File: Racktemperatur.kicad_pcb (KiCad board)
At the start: 2 copper layers, 67.6 x 57.5 mm, 20 parts, among them J1 Conn_01x03, J2 Conn_01x03, J3 Barrel_Jack_MountingPin, Q1 IRLZ44N, U1 74HC595, U2 74HC595, U3 DS18B20

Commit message: Version 1.3 as rack mount
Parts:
- removed the REF** at (145.7, 125.5)
- removed the REF** at (84.4, 125.5)
- added G***: LOGO, libs:Logo, F.Cu at (111.7, 101.7)
- added J4: Screw_Terminal_01x02, TerminalBlock:TerminalBlock_bornier-2_P5.08mm, F.Cu at (187.8, 91.1)
- R1, R2, R3, R4, R5: moved to B.Cu
- moved J3 83.1 mm to (177.9, 98.9), turned to 90 degrees
- moved R4 78.7 mm to (180.1, 117.3)
- moved REF** 65.0 mm to (190.0, 115.4)
- moved R5 61.7 mm to (175.0, 117.3), turned to 90 degrees
- moved R3 58.1 mm to (180.3, 90.8), turned to 180 degrees
- moved U3 56.7 mm to (178.9, 87.5), turned to 0 degrees
- moved U1 56.6 mm to (137.0, 82.8), turned to 0 degrees
- moved J2 52.8 mm to (163.8, 91.8), turned to 270 degrees
- moved J1 52.6 mm to (163.8, 82.9), turned to 270 degrees
- moved U2 52.0 mm to (123.3, 82.8), turned to 0 degrees
- moved Q1 48.8 mm to (151.1, 101.0), turned to 0 degrees
- moved A1 47.6 mm to (152.1, 120.9), turned to 90 degrees
- moved D1 43.8 mm to (164.7, 101.3), turned to 180 degrees
- moved R1 21.2 mm to (140.8, 116.6)
- moved G*** 20.7 mm to (111.7, 101.7), turned to 180 degrees
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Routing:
- net GND: track 66.4 -> 27.7 mm, vias 0 -> 5
- net Net-(A1-Pad27): track 38.8 -> 3.35 mm, vias 1 -> 0
- net Net-(A1-Pad15): track 95.2 -> 60.7 mm, vias 2 -> 1
- net Net-(A1-Pad16): track 0.00 -> 21.1 mm
- net Net-(A1-Pad5): track 24.7 -> 3.67 mm
- net +12V: track 67.6 -> 49.0 mm
- net Net-(A1-Pad10): track 19.7 -> 2.53 mm
- net Net-(D1-Pad2): track 3.26 -> 20.3 mm
- net Net-(A1-Pad13): track 82.3 -> 68.1 mm, vias 0 -> 1
- net Net-(A1-Pad14): track 83.9 -> 70.0 mm, vias 2 -> 0
- net Net-(U1-Pad9): track 19.9 -> 29.6 mm, vias 0 -> 2
- net Net-(A1-Pad17): track 111.4 -> 102.6 mm, vias 0 -> 2
- net Net-(J1-Pad1): track 17.4 -> 24.4 mm
- net Net-(A1-Pad12): track 38.7 -> 45.0 mm, vias 1 -> 3
- net Net-(AFF2-Pad2): track 31.1 -> 34.3 mm
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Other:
- board size 67.6 x 57.5 mm -> 91.8 x 42.7 mm
- board text added: "D2 = DS18B20 1Wire Sensor D7 = LED D9 = Fan PWM (MOSFET) D10 = 7 Seg RCLK D11 = 7 Seg SRCLK D12 = 7 Seg SER D13 = Terminal"
- board text added: "IRLZ44N"
- board text added: "v1.3"
- board text removed: "D2 = DS18B20 1Wire Sensor D7 = LED D9 = Fan PWM (MOSFET) D10 = 7 Seg RCLK D11 = 7 Seg SRCLK D12 = 7 Seg SER"
- board text removed: "v1.2"

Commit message: unconnected item
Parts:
- added REF**: WEEE-Logo_4.2x6mm_SilkScreen, Symbol:WEEE-Logo_4.2x6mm_SilkScreen, F.Cu at (172.0, 88.4)
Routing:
- net Net-(A1-Pad5): track 3.67 -> 48.7 mm, vias 0 -> 2
- net Net-(A1-Pad27): track 3.35 -> 31.8 mm, vias 0 -> 1
- net GND: vias 5 -> 6
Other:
- board text added: "v1.4"
- board text removed: "v1.3"

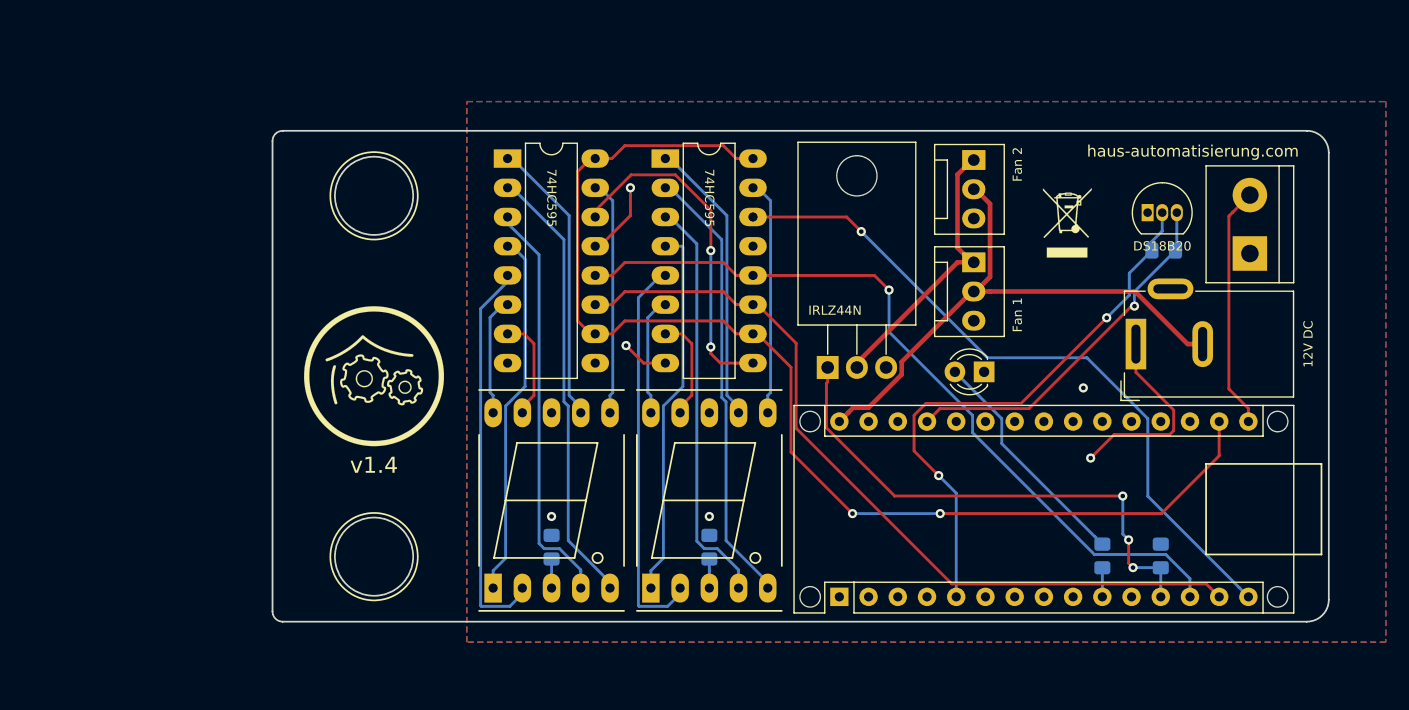
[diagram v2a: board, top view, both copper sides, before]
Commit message: Added LM7805
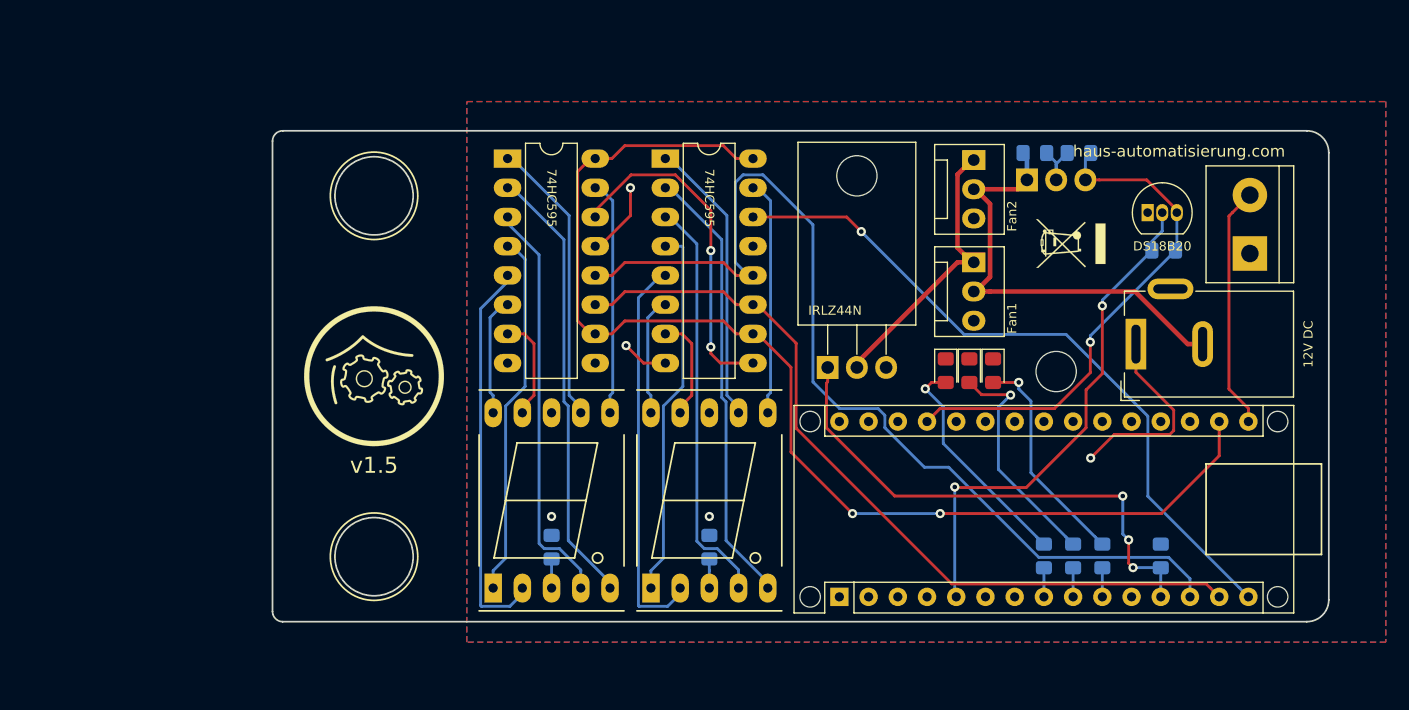
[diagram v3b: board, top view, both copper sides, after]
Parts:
- added C1: C, Capacitor_SMD:C_0805_2012Metric_Pad1.15x1.40mm_HandSolder, B.Cu at (169.1, 82.3)
- added C2: C, Capacitor_SMD:C_0805_2012Metric_Pad1.15x1.40mm_HandSolder, B.Cu at (173.0, 82.3)
- added D2: LED, LED_SMD:LED_0805_2012Metric_Pad1.15x1.40mm_HandSolder, F.Cu at (161.4, 101.2)
- added D3: LED, LED_SMD:LED_0805_2012Metric_Pad1.15x1.40mm_HandSolder, F.Cu at (163.4, 101.2)
- added R6: 330Ω, Resistor_SMD:R_0805_2012Metric_Pad1.15x1.40mm_HandSolder, B.Cu at (169.9, 117.3)
- added R7: 330Ω, Resistor_SMD:R_0805_2012Metric_Pad1.15x1.40mm_HandSolder, B.Cu at (172.5, 117.3)
- added U4: L7805, Package_TO_SOT_THT:TO-220-3_Horizontal_TabDown, B.Cu at (168.5, 84.7)
- D1: footprint LED_THT:LED_D3.0mm -> LED_SMD:LED_0805_2012Metric_Pad1.15x1.40mm_HandSolder
- moved REF** 2.31 mm to (190.3, 113.2)
- moved REF** 1.83 mm to (172.3, 90.2), turned to 90 degrees
- moved D1 0.78 mm to (165.5, 101.2), turned to 270 degrees
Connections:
- net Net-(A1-Pad17) renamed /3V3
- net Net-(A1-Pad27) renamed /5V
- A1 pad 30: +12V -> Net-(A1-Pad30)
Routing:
- net Net-(D3-Pad2): track 0.00 -> 20.1 mm, vias 0 -> 1
- net Net-(A1-Pad13): track 68.1 -> 88.1 mm, vias 1 -> 0
- net Net-(D2-Pad2): track 0.00 -> 19.8 mm, vias 0 -> 1
- net /5V: track 31.8 -> 44.8 mm
- net +12V: track 49.0 -> 39.5 mm
- net GND: track 27.7 -> 33.1 mm, vias 6 -> 5
- net Net-(A1-Pad5): track 48.7 -> 44.6 mm
- net Net-(A1-Pad9): track 0.00 -> 2.53 mm
- net Net-(A1-Pad8): track 0.00 -> 2.53 mm
- net Net-(D1-Pad2): track 20.3 -> 19.3 mm, vias 0 -> 1
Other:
- board text added: "100nF"
- board text added: "D2 = DS18B20 1Wire Sensor D5, D7, D7 = LED D9 = Fan PWM (MOSFET) D10 = 7 Seg RCLK D11 = 7 Seg SRCLK D12 = 7 Seg SER D13 = Terminal"
- board text added: "Fan1"
- board text added: "Fan2"
- board text added: "LM7805"
- board text added: "v1.5"
- board text removed: "D2 = DS18B20 1Wire Sensor D7 = LED D9 = Fan PWM (MOSFET) D10 = 7 Seg RCLK D11 = 7 Seg SRCLK D12 = 7 Seg SER D13 = Terminal"
- board text removed: "Fan 1"
- board text removed: "Fan 2"
- board text removed: "v1.4"

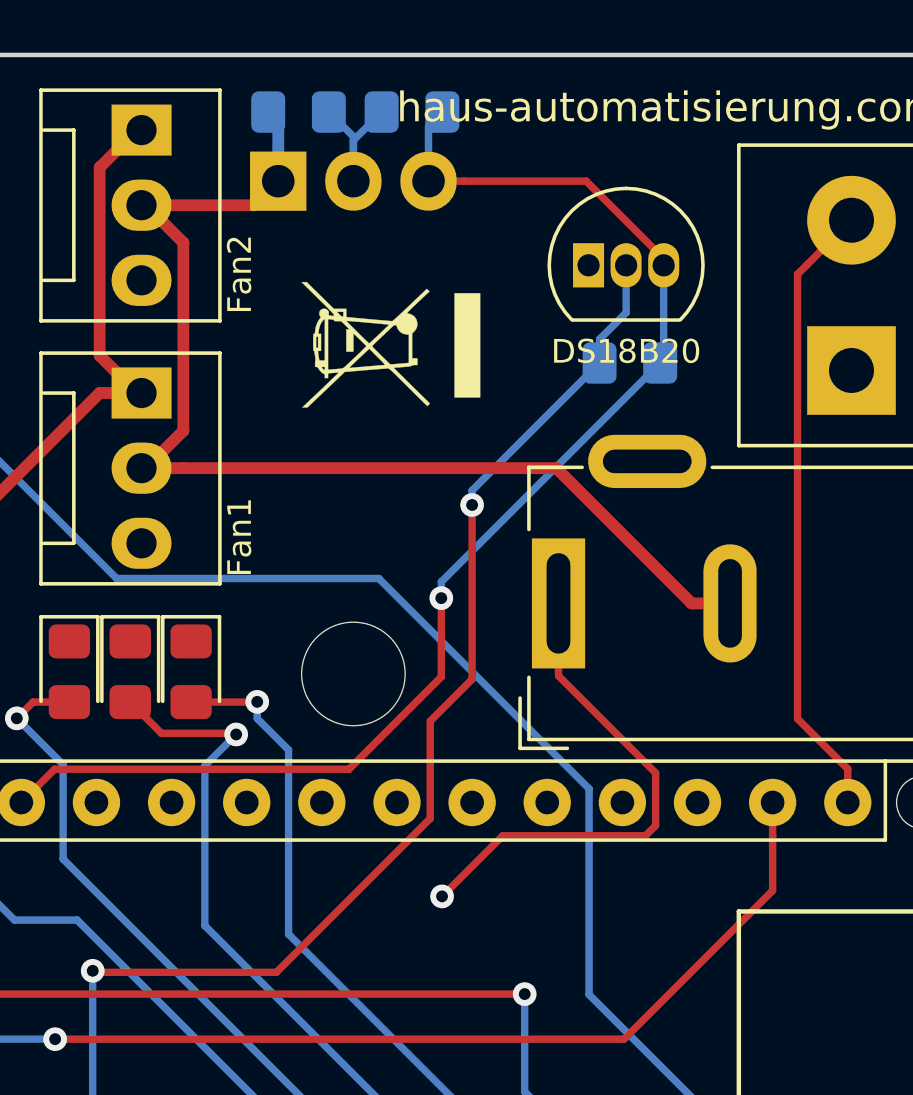
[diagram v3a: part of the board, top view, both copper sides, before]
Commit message: Changed polarity of barrel jack
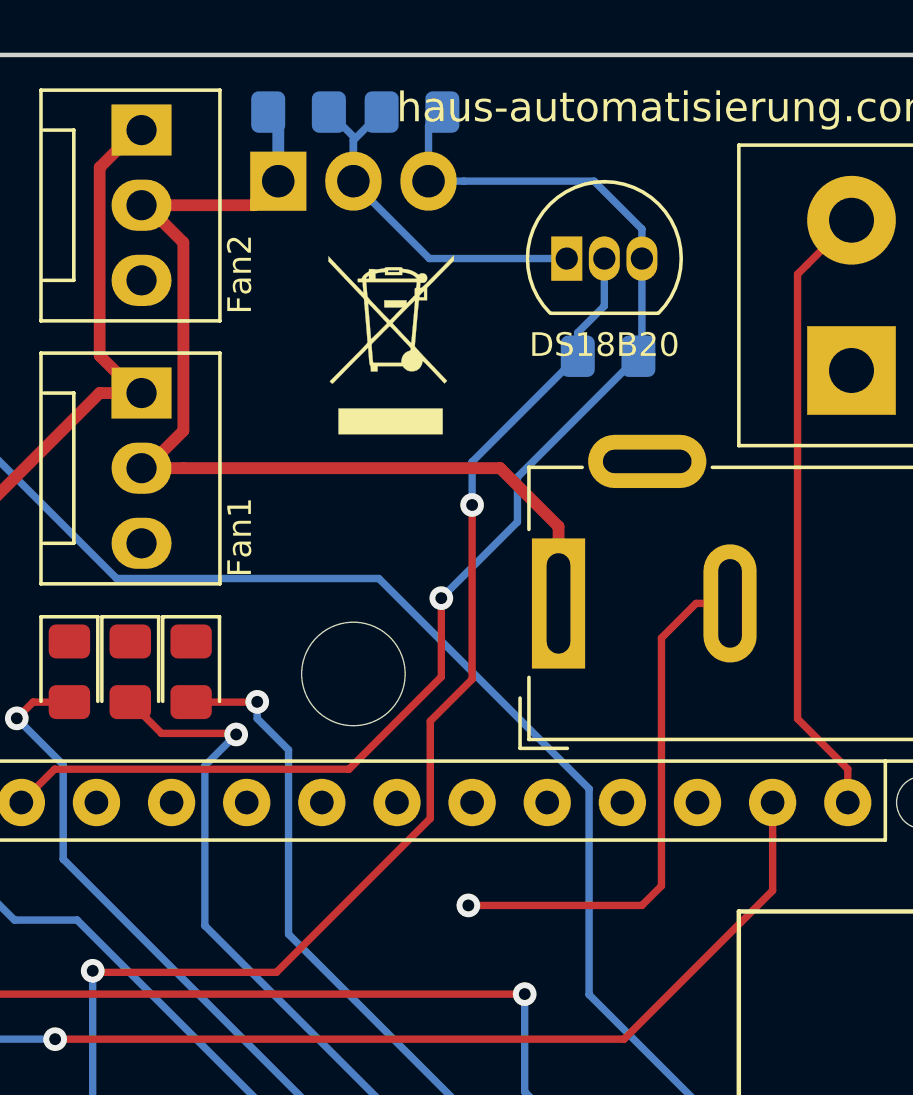
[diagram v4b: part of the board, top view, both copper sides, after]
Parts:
- moved R3 0.77 mm to (179.6, 90.6)
- moved U3 0.77 mm to (178.2, 87.3)
- turned REF** to 0 degrees
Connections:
- J3 pad 1: GND -> +12V
- J3 pad 2: +12V -> GND
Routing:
- net GND: track 33.1 -> 42.4 mm
- net +12V: track 39.5 -> 35.2 mm
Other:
- board text added: "D2 = DS18B20 1Wire Sensor D5, D7, D7 = LED D9 = Fan PWM D10 = 7 Seg RCLK D11 = 7 Seg SRCLK D12 = 7 Seg SER D13 = Terminal"
- board text removed: "D2 = DS18B20 1Wire Sensor D5, D7, D7 = LED D9 = Fan PWM (MOSFET) D10 = 7 Seg RCLK D11 = 7 Seg SRCLK D12 = 7 Seg SER D13 = Terminal"

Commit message: Minor changes
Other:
- board text added: "R Y G"
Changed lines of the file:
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@@
   (general
     (thickness 1.6)
-    (drawings 46)
+    (drawings 47)
     (tracks 304)
     (zones 0)
@@
   (title_block
     (title "Rack Temperature Control")
-    (date 2019-10-26)
+    (date 2019-11-12)
     (rev 1.5)
     (company haus-automatisierung.com)
@@
     )
   )
+  (gr_text "R    Y    G" (at 163.449 103.6828) (layer F.SilkS)
+    (effects (font (size 0.5 0.5) (thickness 0.125)))
+  )
   (gr_text 100nF (at 166.5732 83.185 90) (layer B.SilkS)

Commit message: Added Source Code
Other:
- board text added: "D2 = DS18B20 1Wire Sensor D5, D6, D7 = LED D9 = Fan PWM D10 = 7 Seg RCLK D11 = 7 Seg SRCLK D12 = 7 Seg SER D13 = Terminal"
- board text removed: "D2 = DS18B20 1Wire Sensor D5, D7, D7 = LED D9 = Fan PWM D10 = 7 Seg RCLK D11 = 7 Seg SRCLK D12 = 7 Seg SER D13 = Terminal"
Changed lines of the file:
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@@
     (effects (font (size 0.8 0.8) (thickness 0.15)) (justify mirror))
   )
-  (gr_text "D2 = DS18B20 1Wire Sensor\nD5, D7, D7 = LED\nD9 = Fan PWM\nD10 = 7 Seg RCLK\nD11 = 7 Seg SRCLK\nD12 = 7 Seg SER\nD13 = Terminal" (at 151.6634 88.0364 90) (layer B.SilkS)
+  (gr_text "D2 = DS18B20 1Wire Sensor\nD5, D6, D7 = LED\nD9 = Fan PWM\nD10 = 7 Seg RCLK\nD11 = 7 Seg SRCLK\nD12 = 7 Seg SER\nD13 = Terminal" (at 151.6634 88.0364 90) (layer B.SilkS)
     (effects (font (size 0.7 0.7) (thickness 0.15)) (justify left mirror))
   )

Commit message: Updated to KiCad 6
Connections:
- A1 pad 1: Net-(A1-Pad1) -> unconnected-(A1-Pad1)
- A1 pad 11: Net-(A1-Pad11) -> unconnected-(A1-Pad11)
- A1 pad 18: Net-(A1-Pad18) -> unconnected-(A1-Pad18)
- A1 pad 19: Net-(A1-Pad19) -> unconnected-(A1-Pad19)
- A1 pad 2: Net-(A1-Pad2) -> unconnected-(A1-Pad2)
- A1 pad 20: Net-(A1-Pad20) -> unconnected-(A1-Pad20)
- A1 pad 21: Net-(A1-Pad21) -> unconnected-(A1-Pad21)
- A1 pad 22: Net-(A1-Pad22) -> unconnected-(A1-Pad22)
- A1 pad 23: Net-(A1-Pad23) -> unconnected-(A1-Pad23)
- A1 pad 24: Net-(A1-Pad24) -> unconnected-(A1-Pad24)
- A1 pad 25: Net-(A1-Pad25) -> unconnected-(A1-Pad25)
- A1 pad 26: Net-(A1-Pad26) -> unconnected-(A1-Pad26)
- A1 pad 28: Net-(A1-Pad28) -> unconnected-(A1-Pad28)
- A1 pad 29: Net-(A1-Pad29) -> unconnected-(A1-Pad29)
- A1 pad 3: Net-(A1-Pad3) -> unconnected-(A1-Pad3)
- A1 pad 30: Net-(A1-Pad30) -> unconnected-(A1-Pad30)
- A1 pad 6: Net-(A1-Pad6) -> unconnected-(A1-Pad6)
- A1 pad 7: Net-(A1-Pad7) -> unconnected-(A1-Pad7)
- AFF1 pad 8: Net-(AFF1-Pad8) -> unconnected-(AFF1-Pad8)
- AFF2 pad 8: Net-(AFF2-Pad8) -> unconnected-(AFF2-Pad8)
- J1 pad 3: Net-(J1-Pad3) -> unconnected-(J1-Pad3)
- J2 pad 3: Net-(J2-Pad3) -> unconnected-(J2-Pad3)
- U2 pad 9: Net-(U2-Pad9) -> unconnected-(U2-Pad9)
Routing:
- net Net-(A1-Pad14): track 70.0 -> 70.8 mm
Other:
- net class 12V removed
- net class Default removed

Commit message: v1.6
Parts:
- C1, C2: footprint Capacitor_SMD:C_0805_2012Metric_Pad1.15x1.40mm_HandSolder -> Capacitor_SMD:C_0805_2012Metric_Pad1.18x1.45mm_HandSolder
- R1, R2, R3, R4, R5, R6, R7: footprint Resistor_SMD:R_0805_2012Metric_Pad1.15x1.40mm_HandSolder -> Resistor_SMD:R_0805_2012Metric_Pad1.20x1.40mm_HandSolder
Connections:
- A1 pad 1: unconnected-(A1-Pad1) -> (no net)
- A1 pad 10: Net-(A1-Pad10) -> (no net)
- A1 pad 11: unconnected-(A1-Pad11) -> (no net)
- A1 pad 12: Net-(A1-Pad12) -> (no net)
- A1 pad 13: Net-(A1-Pad13) -> (no net)
- A1 pad 14: Net-(A1-Pad14) -> (no net)
- A1 pad 15: Net-(A1-Pad15) -> (no net)
- A1 pad 16: Net-(A1-Pad16) -> (no net)
- A1 pad 18: unconnected-(A1-Pad18) -> (no net)
- A1 pad 19: unconnected-(A1-Pad19) -> (no net)
- A1 pad 2: unconnected-(A1-Pad2) -> (no net)
- A1 pad 20: unconnected-(A1-Pad20) -> (no net)
- A1 pad 21: unconnected-(A1-Pad21) -> (no net)
- A1 pad 22: unconnected-(A1-Pad22) -> (no net)
- A1 pad 23: unconnected-(A1-Pad23) -> (no net)
- A1 pad 24: unconnected-(A1-Pad24) -> (no net)
- A1 pad 25: unconnected-(A1-Pad25) -> (no net)
- A1 pad 26: unconnected-(A1-Pad26) -> (no net)
- A1 pad 28: unconnected-(A1-Pad28) -> (no net)
- A1 pad 29: unconnected-(A1-Pad29) -> (no net)
- A1 pad 3: unconnected-(A1-Pad3) -> (no net)
- A1 pad 30: unconnected-(A1-Pad30) -> (no net)
- A1 pad 5: Net-(A1-Pad5) -> (no net)
- A1 pad 6: unconnected-(A1-Pad6) -> (no net)
- A1 pad 7: unconnected-(A1-Pad7) -> (no net)
- A1 pad 8: Net-(A1-Pad8) -> (no net)
- A1 pad 9: Net-(A1-Pad9) -> (no net)
- AFF1 pad 1: Net-(AFF1-Pad1) -> (no net)
- AFF1 pad 10: Net-(AFF1-Pad10) -> (no net)
- AFF1 pad 2: Net-(AFF1-Pad2) -> (no net)
- AFF1 pad 3: Net-(AFF1-Pad3) -> (no net)
- AFF1 pad 4: Net-(AFF1-Pad4) -> (no net)
- AFF1 pad 5: Net-(AFF1-Pad5) -> (no net)
- AFF1 pad 6: Net-(AFF1-Pad6) -> (no net)
- AFF1 pad 7: Net-(AFF1-Pad7) -> (no net)
- AFF1 pad 8: unconnected-(AFF1-Pad8) -> (no net)
- AFF1 pad 9: Net-(AFF1-Pad9) -> (no net)
- AFF2 pad 1: Net-(AFF2-Pad1) -> (no net)
- AFF2 pad 10: Net-(AFF2-Pad10) -> (no net)
- AFF2 pad 2: Net-(AFF2-Pad2) -> (no net)
- AFF2 pad 3: Net-(AFF2-Pad3) -> (no net)
- AFF2 pad 4: Net-(AFF2-Pad4) -> (no net)
- AFF2 pad 5: Net-(AFF2-Pad5) -> (no net)
- AFF2 pad 6: Net-(AFF2-Pad6) -> (no net)
- AFF2 pad 7: Net-(AFF2-Pad7) -> (no net)
- AFF2 pad 8: unconnected-(AFF2-Pad8) -> (no net)
- AFF2 pad 9: Net-(AFF2-Pad9) -> (no net)
- D1 pad 2: Net-(D1-Pad2) -> (no net)
- D2 pad 2: Net-(D2-Pad2) -> (no net)
- D3 pad 2: Net-(D3-Pad2) -> (no net)
- J1 pad 1: Net-(J1-Pad1) -> (no net)
- J1 pad 3: unconnected-(J1-Pad3) -> (no net)
- J2 pad 1: Net-(J1-Pad1) -> Net-(J1-Pin_1)
- J2 pad 3: unconnected-(J2-Pad3) -> (no net)
- J4 pad 2: Net-(A1-Pad16) -> Net-(A1-D13)
- Q1 pad 1: Net-(A1-Pad12) -> Net-(A1-D9)
- Q1 pad 2: Net-(J1-Pad1) -> Net-(J1-Pin_1)
- R1 pad 1: Net-(AFF1-Pad3) -> Net-(AFF1-C.K.-Pad3)
- R2 pad 1: Net-(AFF2-Pad3) -> Net-(AFF2-C.K.-Pad3)
- R3 pad 2: Net-(A1-Pad5) -> Net-(A1-D2)
- R4 pad 1: Net-(A1-Pad12) -> Net-(A1-D9)
- R5 pad 1: Net-(A1-Pad10) -> Net-(A1-D7)
- R5 pad 2: Net-(D1-Pad2) -> Net-(D1-A)
- R6 pad 1: Net-(A1-Pad8) -> Net-(A1-D5)
- R6 pad 2: Net-(D2-Pad2) -> Net-(D2-A)
- R7 pad 1: Net-(A1-Pad9) -> Net-(A1-D6)
- R7 pad 2: Net-(D3-Pad2) -> Net-(D3-A)
- U1 pad 1: Net-(AFF1-Pad7) -> Net-(AFF1-a)
- U1 pad 11: Net-(A1-Pad14) -> Net-(A1-D11)
- U1 pad 12: Net-(A1-Pad13) -> Net-(A1-D10)
- U1 pad 14: Net-(A1-Pad15) -> Net-(A1-D12)
- U1 pad 15: Net-(AFF1-Pad6) -> Net-(AFF1-b)
- U1 pad 2: Net-(AFF1-Pad5) -> Net-(AFF1-DP)
- U1 pad 3: Net-(AFF1-Pad4) -> Net-(AFF1-c)
- U1 pad 4: Net-(AFF1-Pad1) -> Net-(AFF1-e)
- U1 pad 5: Net-(AFF1-Pad2) -> Net-(AFF1-d)
- U1 pad 6: Net-(AFF1-Pad10) -> Net-(AFF1-g)
- U1 pad 7: Net-(AFF1-Pad9) -> Net-(AFF1-f)
- U1 pad 9: Net-(U1-Pad9) -> (no net)
- U2 pad 1: Net-(AFF2-Pad7) -> Net-(AFF2-a)
- U2 pad 11: Net-(A1-Pad14) -> Net-(A1-D11)
- U2 pad 12: Net-(A1-Pad13) -> Net-(A1-D10)
- U2 pad 14: Net-(U1-Pad9) -> Net-(U1-QH')
- U2 pad 15: Net-(AFF2-Pad6) -> Net-(AFF2-b)
- U2 pad 2: Net-(AFF2-Pad5) -> Net-(AFF2-DP)
- U2 pad 3: Net-(AFF2-Pad4) -> Net-(AFF2-c)
- U2 pad 4: Net-(AFF2-Pad1) -> Net-(AFF2-e)
- U2 pad 5: Net-(AFF2-Pad2) -> Net-(AFF2-d)
- U2 pad 6: Net-(AFF2-Pad10) -> Net-(AFF2-g)
- U2 pad 7: Net-(AFF2-Pad9) -> Net-(AFF2-f)
- U2 pad 9: unconnected-(U2-Pad9) -> (no net)
- U3 pad 2: Net-(A1-Pad5) -> Net-(A1-D2)
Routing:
- net Net-(A1-Pad13): track 88.1 -> 0.00 mm
- net Net-(A1-D10): track 0.00 -> 88.1 mm
- net Net-(A1-Pad14): track 70.8 -> 0.00 mm
- net Net-(A1-D11): track 0.00 -> 70.8 mm
- net Net-(A1-Pad15): track 60.8 -> 0.00 mm, vias 1 -> 0
- net Net-(A1-D12): track 0.00 -> 60.8 mm, vias 0 -> 1
- net Net-(A1-Pad12): track 45.0 -> 0.00 mm, vias 3 -> 0
- net Net-(A1-D9): track 0.00 -> 45.0 mm, vias 0 -> 3
- net Net-(A1-Pad5): track 44.6 -> 0.00 mm, vias 2 -> 0
- net Net-(A1-D2): track 0.00 -> 44.6 mm, vias 0 -> 2
- net Net-(AFF1-Pad5): track 38.7 -> 0.00 mm
- net Net-(AFF1-DP): track 0.00 -> 38.7 mm
- net Net-(AFF2-Pad5): track 38.7 -> 0.00 mm
- net Net-(AFF2-DP): track 0.00 -> 38.7 mm
- net Net-(AFF1-c): track 0.00 -> 35.8 mm
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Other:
- board text added: "v1.6"
- board text removed: "v1.5"
